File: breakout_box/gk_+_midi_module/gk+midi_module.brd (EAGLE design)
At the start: 65.2 x 100 mm, 113 parts, among them T1 2N2222, T2 2N2222, U2 LMV324, U3 TLV2170DGKT, U4 L78LXX, U5 MIC5205-3.3, U6 MSP430G2553RHB32, X1 QUARZ5

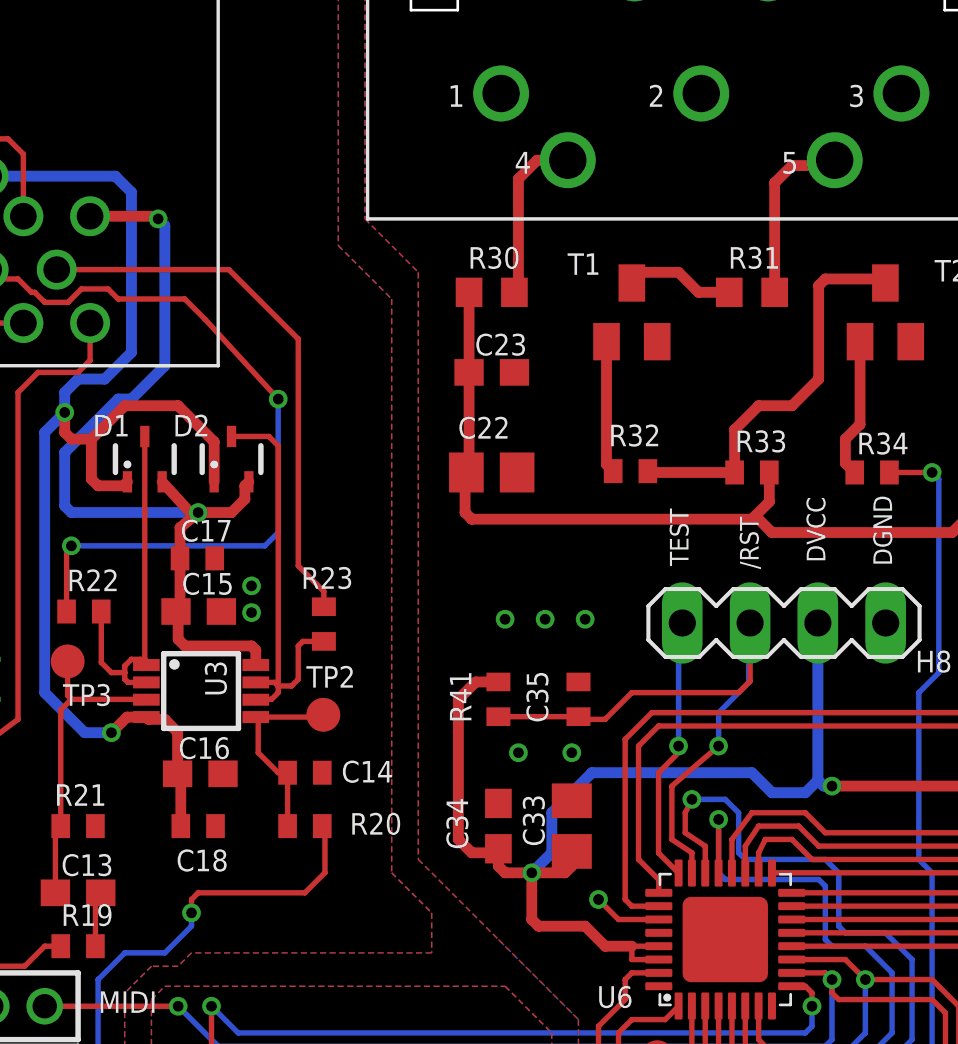
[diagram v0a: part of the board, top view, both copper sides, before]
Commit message: Update brd and sch file with corrected footprints
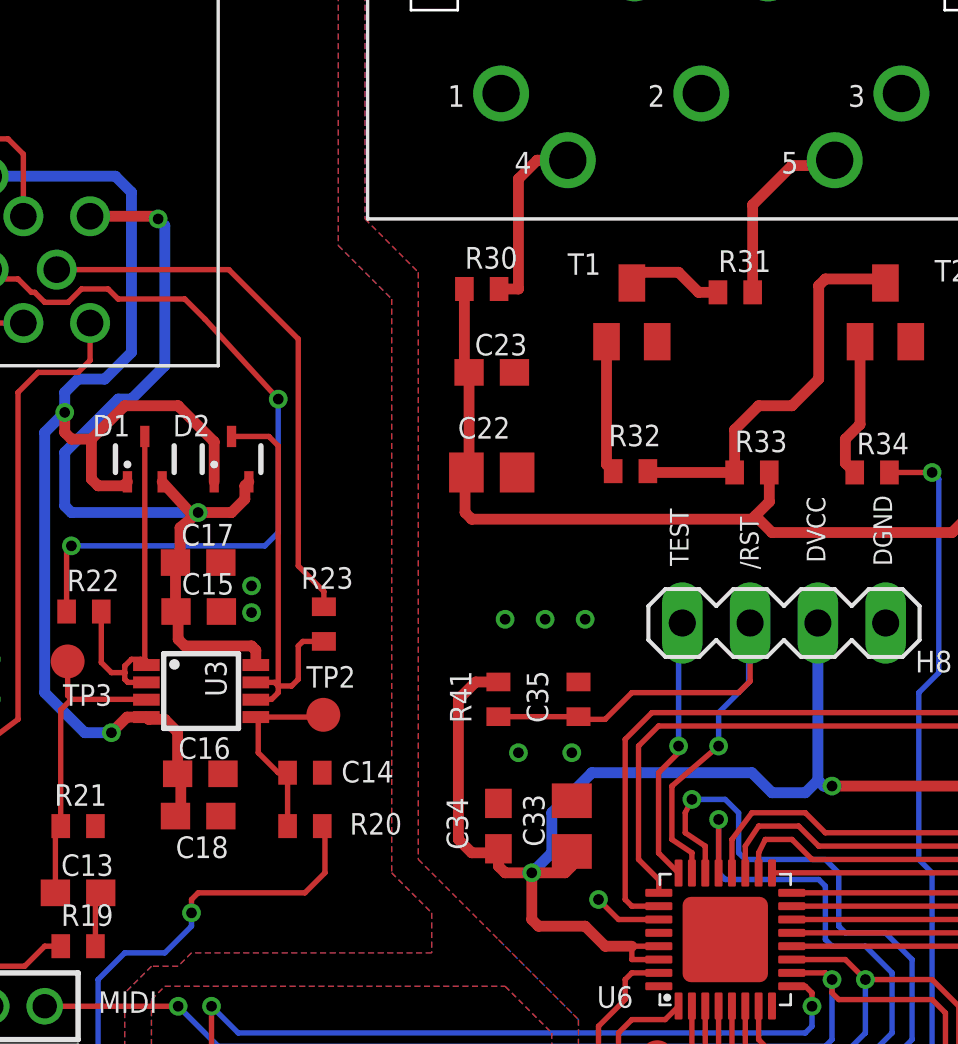
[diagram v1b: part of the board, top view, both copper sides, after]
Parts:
- C17, C18: device resistor:C0402 -> resistor:C0603
- R30, R31: value 220R -> 220; device resistor:R0603 -> resistor:R0402
- moved R31 0.62 mm to (42.4, 82.8)
- moved R30 0.40 mm to (32.9, 82.9)
- moved C18 0.38 mm to (22.2, 63.1)
- moved C17 0.16 mm to (22.2, 72.6)
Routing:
- net N$5: track 6.45 -> 6.99 mm

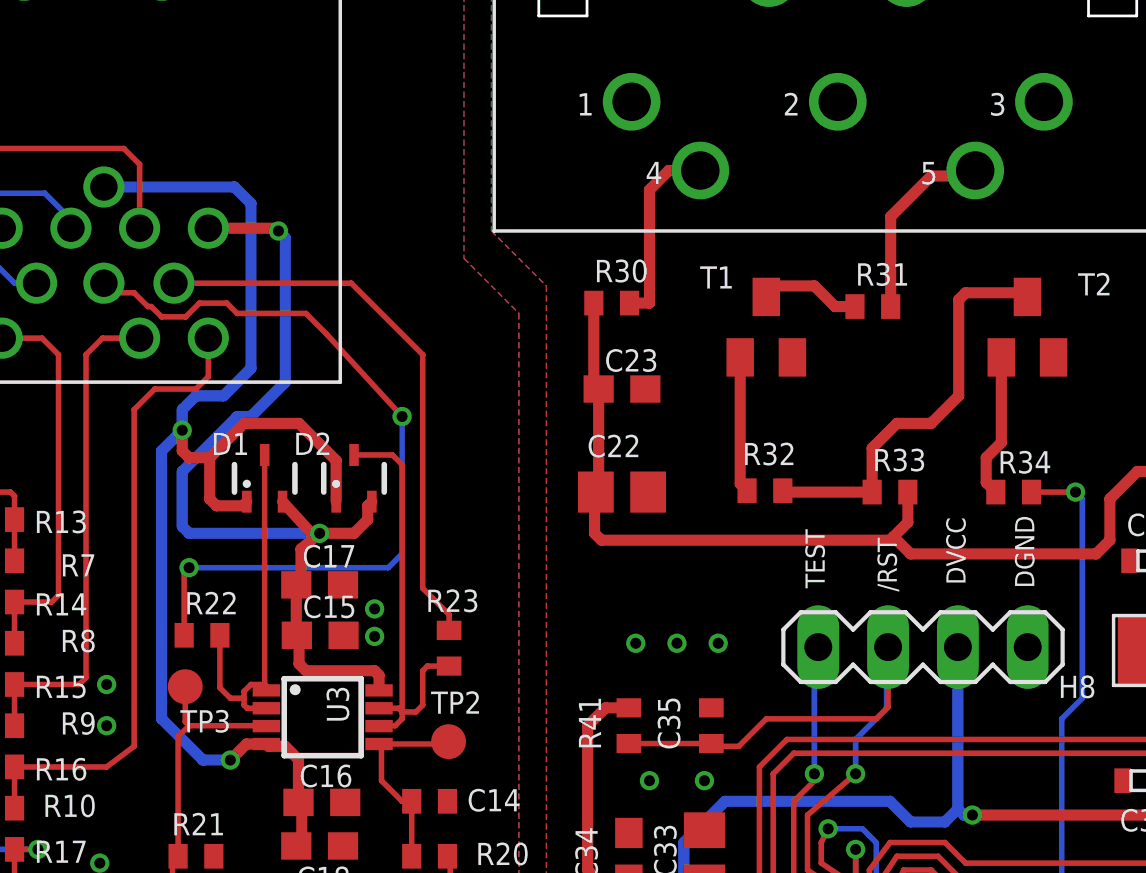
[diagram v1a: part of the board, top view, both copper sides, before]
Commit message: changed some resistors to 0603
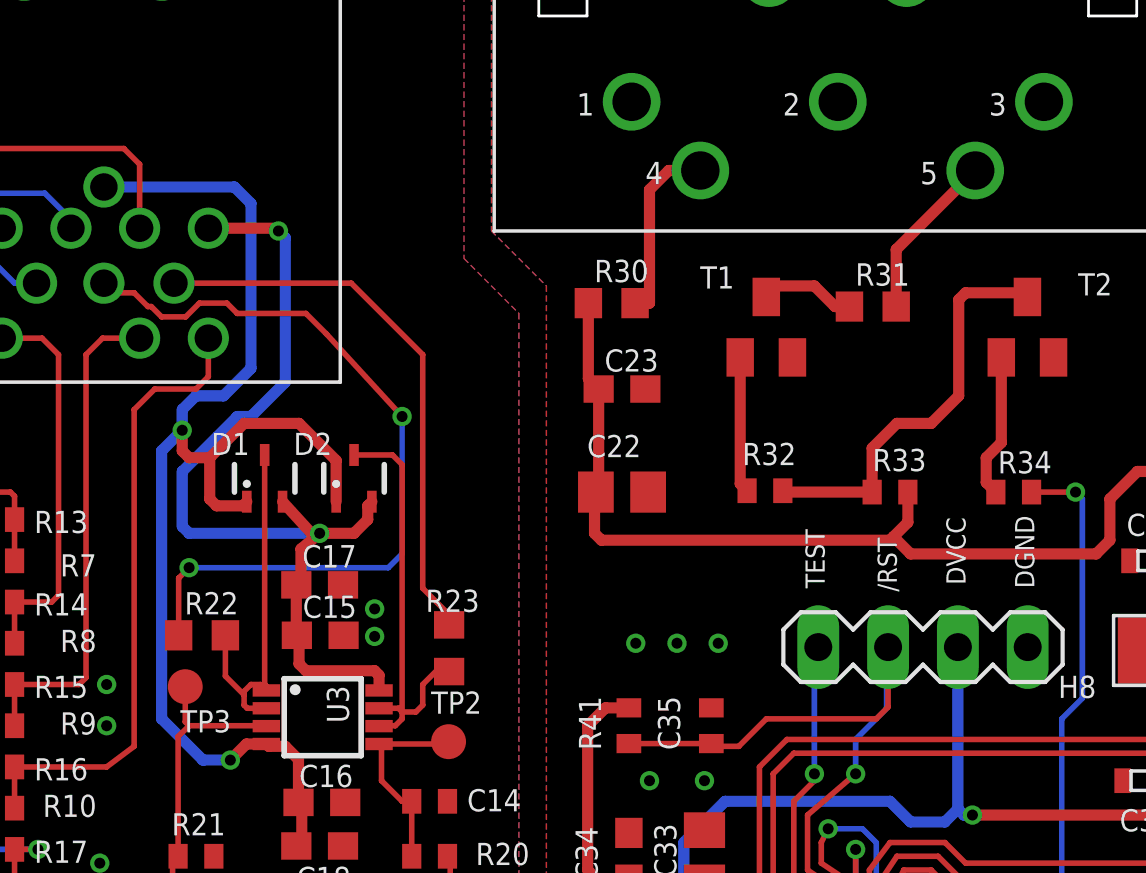
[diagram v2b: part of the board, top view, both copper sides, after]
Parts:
- R22, R23, R30, R31: device resistor:R0402 -> resistor:R0603
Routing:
- net N$1: track 7.04 -> 6.42 mm
- net N$39: track 13.9 -> 13.4 mm
